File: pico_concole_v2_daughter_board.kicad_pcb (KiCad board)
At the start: 2 copper layers, 165.1 x 95.2 mm, 225 parts, among them J1 SM03B-SRSS-TB, J2 SM03B-SRSS-TB, J3 USB_C_Receptacle_USB2.0_16P, J4 Conn_02x12, J5 Conn_02x12, J6 Conn_01x10_MountingPin, J7 Conn_01x04_MountingPin, Q1 SS8050, SW1 SW_Push, SW10 SW_Push, SW11 SW_Push, SW12 SW_Push, SW13 SW_Push, SW14 SW_Push, SW15 SW_Push, SW16 SW_Push, SW17 SW_Push, SW18 SW_Push, SW19 SW_Push, SW2 SW_Push, SW3 SW_Push, SW4 SW_Push, SW5 SW_Push, SW6 SW_Push, SW7 SW_Push, SW8 SW_Push, SW9 SW_Push, U1 USBLC6-2SC6, U10 BQ25619, U2 RP2350_80QFN, U3 W25Q16JVSS, U4 TSOP34S40F, U5 XPT2046TS, U6 PCM5102A, U7 PAM8403D, U8 PAM8403D, U9 MPU-6050, Y1 ABM8-272-T3

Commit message: Update BOM
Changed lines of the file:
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@@
 		(sheetname "/Daughterboard/")
 		(sheetfile "Daughterboard.kicad_sch")
-		(attr through_hole)
+		(attr through_hole exclude_from_bom)
 		(fp_line
 			(start 5.5 -1)
@@
 		(sheetname "/Daughterboard/")
 		(sheetfile "Daughterboard.kicad_sch")
-		(attr through_hole)
+		(attr through_hole exclude_from_bom)
 		(fp_line
 			(start 1 5.5)
@@
 		(sheetname "/Daughterboard/")
 		(sheetfile "Daughterboard.kicad_sch")
-		(attr through_hole)
+		(attr through_hole exclude_from_bom)
 		(fp_line
 			(start 6.75 3)
@@
 		(sheetname "/Daughterboard/")
 		(sheetfile "Daughterboard.kicad_sch")
-		(attr through_hole)
+		(attr through_hole exclude_from_bom)
 		(fp_line
 			(start 5.5 -1)
@@
 		(sheetname "/Daughterboard/")
 		(sheetfile "Daughterboard.kicad_sch")
-		(attr through_hole)
+		(attr through_hole exclude_from_bom)
 		(fp_line
 			(start 5.5 -1)
@@
 		(sheetname "/Daughterboard/")
 		(sheetfile "Daughterboard.kicad_sch")
-		(attr through_hole)
+		(attr through_hole exclude_from_bom)
 		(fp_line
 			(start -1.599999 -12.7)
@@
 		(sheetname "/Daughterboard/")
 		(sheetfile "Daughterboard.kicad_sch")
-		(attr through_hole)
+		(attr through_hole exclude_from_bom)
 		(fp_line
 			(start 6.75 3)
@@
 		(sheetname "/Daughterboard/")
 		(sheetfile "Daughterboard.kicad_sch")
-		(attr through_hole)
+		(attr through_hole exclude_from_bom)
 		(fp_line
 			(start -0.25 1.5)
@@
 		(sheetname "/Daughterboard/")
 		(sheetfile "Daughterboard.kicad_sch")
-		(attr through_hole)
+		(attr through_hole exclude_from_bom)
 		(fp_line
 			(start -0.25 1.5)
@@
 		(sheetname "/Daughterboard/")
 		(sheetfile "Daughterboard.kicad_sch")
-		(attr through_hole)
+		(attr through_hole exclude_from_bom)
 		(fp_line
 			(start 1 5.5)
@@
 		(sheetname "/Daughterboard/")
 		(sheetfile "Daughterboard.kicad_sch")
-		(attr through_hole)
+		(attr through_hole exclude_from_bom)
 		(fp_line
 			(start -0.25 1.5)
@@
 		(sheetname "/Daughterboard/")
 		(sheetfile "Daughterboard.kicad_sch")
-		(attr through_hole)
+		(attr through_hole exclude_from_bom)
 		(fp_line
 			(start -18.2 -12.4)
@@
 		(sheetname "/Daughterboard/")
 		(sheetfile "Daughterboard.kicad_sch")
-		(attr through_hole)
+		(attr through_hole exclude_from_bom)
 		(fp_line
 			(start 1 5.5)
@@
 			(at 0 -1.8 90)
 			(layer "F.SilkS")
+			(hide yes)
 			(effects
 				(font
@@
 		(sheetname "/Daughterboard/")
 		(sheetfile "Daughterboard.kicad_sch")
-		(attr through_hole)
+		(attr through_hole exclude_from_bom)
 		(fp_line
 			(start -0.25 1.5)
@@
 		(sheetname "/Daughterboard/")
 		(sheetfile "Daughterboard.kicad_sch")
-		(attr smd exclude_from_bom)
+		(attr smd)
 		(fp_line
 			(start -0.167621 0.38)
@@
 		(sheetname "/Daughterboard/")
 		(sheetfile "Daughterboard.kicad_sch")
-		(attr smd exclude_from_bom)
+		(attr smd)
 		(fp_line
 			(start -0.167621 -0.38)
@@
 		(sheetname "/Daughterboard/")
 		(sheetfile "Daughterboard.kicad_sch")
-		(attr smd exclude_from_bom)
+		(attr smd)
 		(fp_line
 			(start -0.167621 0.38)
@@
 		(sheetname "/Daughterboard/")
 		(sheetfile "Daughterboard.kicad_sch")
-		(attr through_hole)
+		(attr through_hole exclude_from_bom)
 		(fp_line
 			(start 1.599999 12.7)
@@
 		(sheetname "/Daughterboard/")
 		(sheetfile "Daughterboard.kicad_sch")
-		(attr smd exclude_from_bom)
+		(attr smd)
 		(fp_line
 			(start -0.167621 0.38)
@@
 		(sheetname "/Daughterboard/")
 		(sheetfile "Daughterboard.kicad_sch")
-		(attr smd exclude_from_bom)
+		(attr smd)
 		(fp_line
 			(start -0.167621 0.38)
@@
 		(sheetname "/Daughterboard/")
 		(sheetfile "Daughterboard.kicad_sch")
-		(attr smd exclude_from_bom)
+		(attr smd)
 		(fp_line
 			(start -0.167621 0.38)
@@
 			)
 		)
+		(property "LCSC PN" "C177225"
+			(at 0 0 270)
+			(unlocked yes)
+			(layer "B.Fab")
+			(hide yes)
+			(effects
+				(font
+					(size 1 1)
+					(thickness 0.15)
+				)
+				(justify mirror)
+			)
+		)
 		(property ki_fp_filters "Connector*:*_1x??-1MP*")
 		(sheetname "/Daughterboard/")
@@
 			)
 		)
+		(property "LCSC PN" "C177225"
+			(at 0 0 270)
+			(unlocked yes)
+			(layer "B.Fab")
+			(hide yes)
+			(effects
+				(font
+					(size 1 1)
+					(thickness 0.15)
+				)
+				(justify mirror)
+			)
+		)
 		(property ki_fp_filters "Connector*:*_1x??-1MP*")
 		(sheetname "/Daughterboard/")
@@
 		(sheetname "/Daughterboard/")
 		(sheetfile "Daughterboard.kicad_sch")
-		(attr smd exclude_from_bom)
+		(attr smd)
 		(fp_line
 			(start -0.167621 0.38)
@@
 		(sheetname "/Southbridge/")
 		(sheetfile "Southbridge.kicad_sch")
-		(attr smd exclude_from_bom)
+		(attr smd)
 		(fp_line
 			(start -0.167621 -0.38)
@@
 		(sheetname "/Daughterboard/")
 		(sheetfile "Daughterboard.kicad_sch")
-		(attr smd exclude_from_bom)
+		(attr smd)
 		(fp_line
 			(start -0.167621 0.38)
@@
 			)
 		)
+		(property "LCSC PN" "C177225"
+			(at 0 0 90)
+			(unlocked yes)
+			(layer "B.Fab")
+			(hide yes)
+			(effects
+				(font
+					(size 1 1)
+					(thickness 0.15)
+				)
+				(justify mirror)
+			)
+		)
 		(property ki_fp_filters "Connector*:*_1x??-1MP*")
 		(sheetname "/Daughterboard/")
@@
 		(sheetname "/Daughterboard/")
 		(sheetfile "Daughterboard.kicad_sch")
-		(attr smd exclude_from_bom)
+		(attr smd)
 		(fp_line
 			(start -0.167621 -0.38)
@@
 		(sheetname "/Southbridge/")
 		(sheetfile "Southbridge.kicad_sch")
-		(attr smd)
+		(attr smd exclude_from_bom)
 		(fp_line
 			(start -0.227064 -0.735)
@@
 		(sheetname "/Daughterboard/")
 		(sheetfile "Daughterboard.kicad_sch")
-		(attr smd exclude_from_bom)
+		(attr smd)
 		(fp_line
 			(start -0.167621 0.38)
@@
 		(sheetname "/Daughterboard/")
 		(sheetfile "Daughterboard.kicad_sch")
-		(attr smd exclude_from_bom)
+		(attr smd)
 		(fp_line
 			(start -0.167621 -0.38)
@@
 			)
 		)
+		(property "LCSC PN" "C160404"
+			(at 0 0 0)
+			(unlocked yes)
+			(layer "B.Fab")
+			(hide yes)
+			(effects
+				(font
+					(size 1 1)
+					(thickness 0.15)
+				)
+				(justify mirror)
+			)
+		)
 		(property ki_fp_filters "Connector*:*_1x??-1MP*")
 		(sheetname "/Daughterboard/")
@@
 		(sheetname "/Daughterboard/")
 		(sheetfile "Daughterboard.kicad_sch")
-		(attr smd exclude_from_bom)
+		(attr smd)
 		(fp_line
 			(start -0.167621 -0.38)
@@
 			)
 		)
+		(property "LCSC PN" "C177225"
+			(at 0 0 180)
+			(unlocked yes)
+			(layer "B.Fab")
+			(hide yes)
+			(effects
+				(font
+					(size 1 1)
+					(thickness 0.15)
+				)
+				(justify mirror)
+			)
+		)
 		(property ki_fp_filters "Connector*:*_1x??-1MP*")
 		(sheetname "/Daughterboard/")
@@
 		(sheetname "/Southbridge/")
 		(sheetfile "Southbridge.kicad_sch")
-		(attr smd)
+		(attr smd exclude_from_bom)
 		(fp_line
 			(start -0.227064 0.735)
@@
 		(sheetname "/Daughterboard/")
 		(sheetfile "Daughterboard.kicad_sch")
-		(attr smd exclude_from_bom)
+		(attr smd)
 		(fp_line
 			(start -0.167621 -0.38)
@@
 		(sheetname "/Daughterboard/")
 		(sheetfile "Daughterboard.kicad_sch")
-		(attr smd exclude_from_bom)
+		(attr smd)
 		(fp_line
 			(start -0.167621 0.38)
@@
 		(sheetname "/Daughterboard/")
 		(sheetfile "Daughterboard.kicad_sch")
-		(attr smd exclude_from_bom)
+		(attr smd)
 		(fp_line
 			(start -0.167621 -0.38)
@@
 		(sheetname "/Daughterboard/")
 		(sheetfile "Daughterboard.kicad_sch")
-		(attr through_hole)
+		(attr through_hole exclude_from_bom)
 		(fp_line
 			(start 0.04 -2.3)
@@
 		(sheetname "/Southbridge/")
 		(sheetfile "Southbridge.kicad_sch")
-		(attr smd exclude_from_bom)
+		(attr smd)
 		(fp_line
 			(start -0.167621 0.38)
@@
 			)
 		)
+		(property "LCSC PN" "C177225"
+			(at 0 0 180)
+			(unlocked yes)
+			(layer "B.Fab")
+			(hide yes)
+			(effects
+				(font
+					(size 1 1)
+					(thickness 0.15)
+				)
+				(justify mirror)
+			)
+		)
 		(property ki_fp_filters "Connector*:*_1x??-1MP*")
 		(sheetname "/Daughterboard/")
@@
 		(sheetname "/Daughterboard/")
 		(sheetfile "Daughterboard.kicad_sch")
-		(attr through_hole)
+		(attr through_hole exclude_from_bom)
 		(fp_line
 			(start 18.2 12.4)
@@
 		(sheetname "/Daughterboard/")
 		(sheetfile "Daughterboard.kicad_sch")
-		(attr smd exclude_from_bom)
+		(attr smd)
 		(fp_line
 			(start -0.167621 -0.38)
@@
 		(sheetname "/Daughterboard/")
 		(sheetfile "Daughterboard.kicad_sch")
-		(attr smd exclude_from_bom)
+		(attr smd)
 		(fp_line
 			(start -0.167621 -0.38)
@@
 		(sheetname "/Daughterboard/")
 		(sheetfile "Daughterboard.kicad_sch")
-		(attr through_hole)
+		(attr through_hole exclude_from_bom)
 		(fp_line
 			(start -1.29 -1.21)
@@
 		(sheetname "/Daughterboard/")
 		(sheetfile "Daughterboard.kicad_sch")
-		(attr smd exclude_from_bom)
+		(attr smd)
 		(fp_line
 			(start -0.167621 0.38)
@@
 			)
 		)
+		(property "LCSC PN" "C42415655"
+			(at 0 0 0)
+			(unlocked yes)
+			(layer "B.Fab")
+			(hide yes)
+			(effects
+				(font
+					(size 1 1)
+					(thickness 0.15)
+				)
+				(justify mirror)
+			)
+		)
 		(sheetname "/Southbridge/")
 		(sheetfile "Southbridge.kicad_sch")
@@
 		(sheetname "/Southbridge/")
 		(sheetfile "Southbridge.kicad_sch")
-		(attr smd exclude_from_bom)
+		(attr smd)
 		(fp_line
 			(start -0.167621 -0.38)
@@
 		(sheetname "/Daughterboard/")
 		(sheetfile "Daughterboard.kicad_sch")
-		(attr smd exclude_from_bom)
+		(attr smd)
 		(fp_line
 			(start -0.167621 -0.38)
@@
 		(sheetname "/Daughterboard/")
 		(sheetfile "Daughterboard.kicad_sch")
-		(attr smd exclude_from_bom)
+		(attr smd)
 		(fp_line
 			(start -0.167621 0.38)
@@
 		(sheetname "/Daughterboard/")
 		(sheetfile "Daughterboard.kicad_sch")
-		(attr smd exclude_from_bom)
+		(attr smd)
 		(fp_line
 			(start -0.167621 0.38)
@@
 					(thickness 0.15)
 				)
+				(justify mirror)
+			)
+		)
+		(property "LCSC PN" "C177225"
+			(at 0 0 90)
+			(unlocked yes)
+			(layer "B.Fab")
+			(hide yes)
+			(effects
+				(font
+					(size 1 1)
+					(thickness 0.15)
+				)

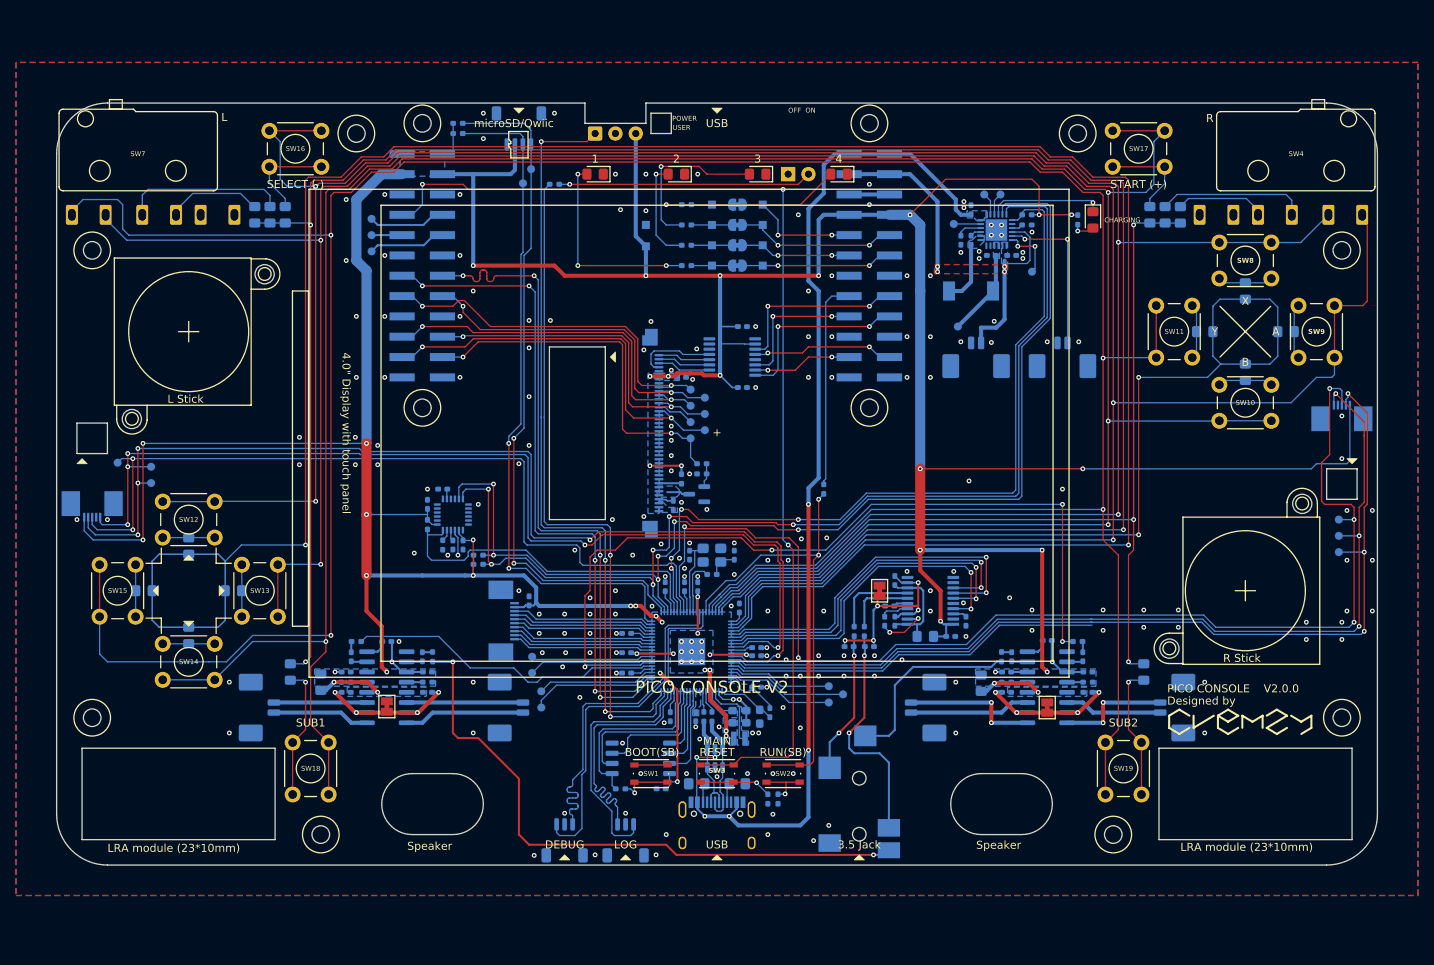
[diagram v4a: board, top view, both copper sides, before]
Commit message: Update schematic - Change L2 - Add NTC2 pad - Connect pins to measure voltages
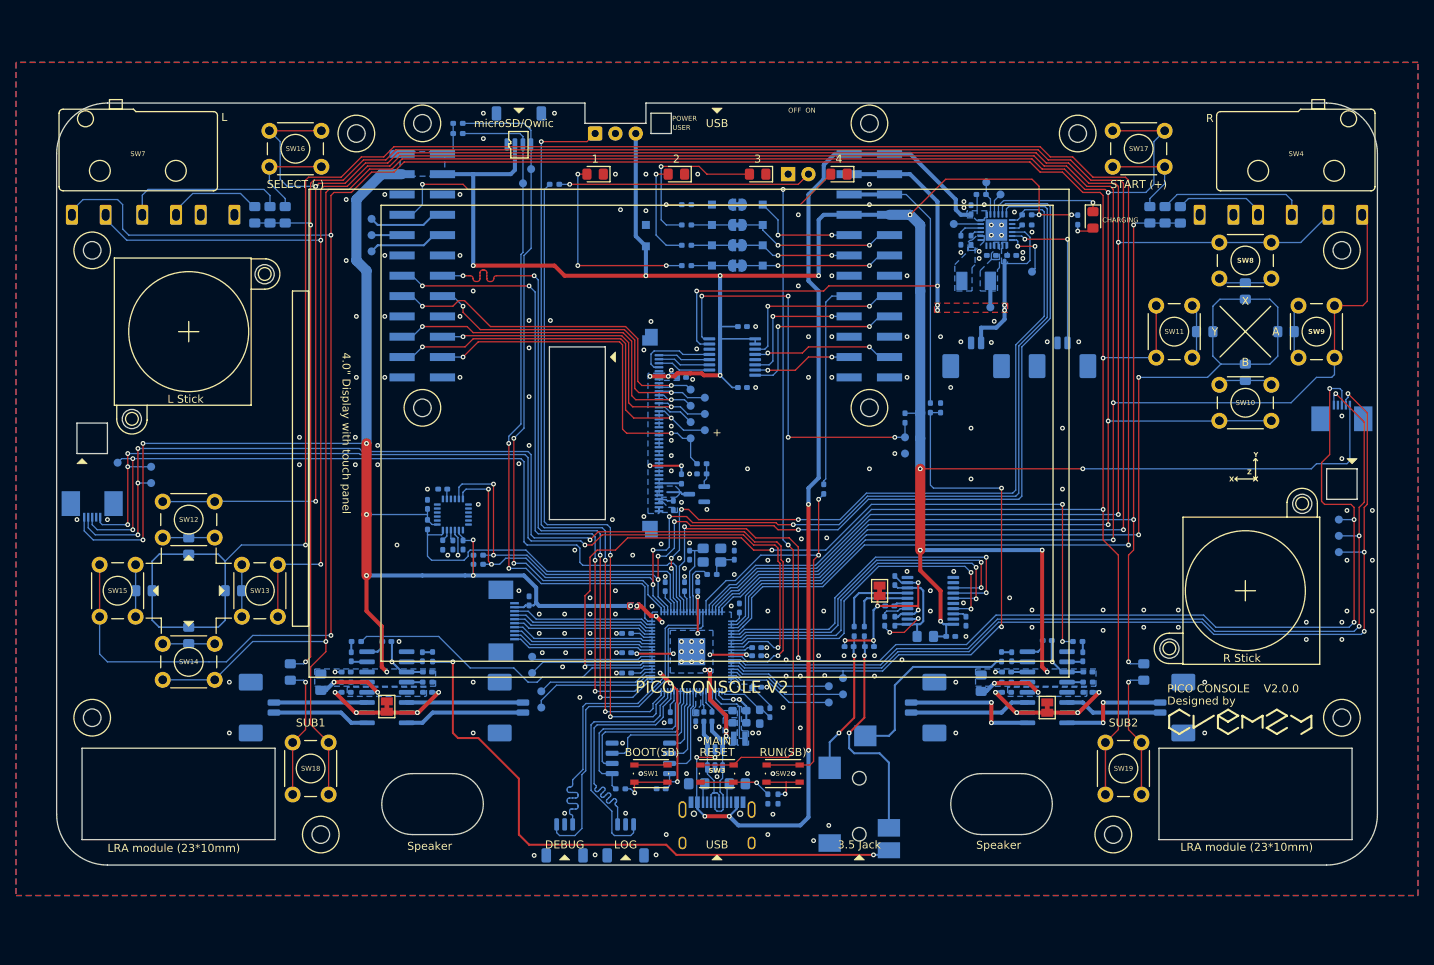
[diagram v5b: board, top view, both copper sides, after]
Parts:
- added R38: 10k, Resistor_SMD:R_0402_1005Metric_Pad0.72x0.64mm_HandSolder, B.Cu at (131.4, 64.8)
- added R39: 10k, Resistor_SMD:R_0402_1005Metric_Pad0.72x0.64mm_HandSolder, B.Cu at (141.0, 36.8)
- added R40: 10k, Resistor_SMD:R_0402_1005Metric_Pad0.72x0.64mm_HandSolder, B.Cu at (135.9, 63.5)
- added R41: 10k, Resistor_SMD:R_0402_1005Metric_Pad0.72x0.64mm_HandSolder, B.Cu at (134.6, 63.5)
- added TP41: TP, TestPoint:TestPoint_Pad_D1.0mm, B.Cu at (131.4, 67.2)
- added TP42: TP, TestPoint:TestPoint_Pad_D1.0mm, B.Cu at (131.4, 69.2)
- added TP43: TP, TestPoint:TestPoint_Pad_D1.0mm, B.Cu at (123.7, 97.3)
- AUDIO1: value AudioJack3_SwitchTR -> SJ2-35954B-SMT-TR
- L2: value 1u -> MAPM0420F-2R2M-LF; footprint Inductor_SMD:L_6.3x6.3_H3 -> Library:Inductor_SMD_L_4.9x4.4_H2
- moved TP39 4.73 mm to (142.1, 50.9)
- moved TP37 1.55 mm to (141.6, 35.3)
- moved L2 1.42 mm to (140.3, 47.6)
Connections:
- net /Daughterboard/BAT_TEMP renamed /Daughterboard/BAT_TEMP1
- U5 pad 7: unconnected-(U5-VBAT-Pad7) -> VBAT
- U5 pad 8: unconnected-(U5-IN-Pad8) -> /Daughterboard/BAT_TEMP2
- U5 pad 9: unconnected-(U5-VREF-Pad9) -> +3V3
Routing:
- net /Daughterboard/BAT_TEMP2: track 0.00 -> 51.0 mm, vias 0 -> 4
- net VBAT: track 43.0 -> 86.1 mm, vias 4 -> 6
- net VIN: track 5.05 -> 34.5 mm
- net /Daughterboard/GPIO44: track 47.7 -> 73.9 mm, vias 0 -> 2
- net BAT_SW: track 7.86 -> 0.00 mm
- net VSYS: track 10.9 -> 3.30 mm
- net VUSB: track 133.4 -> 135.9 mm
- net +3V3: track 551.7 -> 554.1 mm
- net Net-(U10-PSEL): track 2.82 -> 4.27 mm
- net GND: vias 216 -> 221
- added copper zone on F.Cu, net +3V3
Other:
- board text added: "GPIO44"
- board text added: "NTC2"
